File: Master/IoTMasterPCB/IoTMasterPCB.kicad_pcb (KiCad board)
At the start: 4 copper layers, 139 parts, among them J1 M50-3610742R, J2 10118194-0001LF, J3 RJMG1BD3B8K1ANR, U1 STM32F469IITx, U2 MYRGP330100B21RA, U3 CLRC66303HNY, U4 AT86RF232-ZX, U5 MIC826TYMT-TR, U6 KSZ8081MNX, U7 W25Q32JVSS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

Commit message: Placed STM32 on Master PCB. Corrected I2C naming.
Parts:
- moved R19 130.0 mm to (161.7, 60.6), turned to 180 degrees
- moved C18 128.4 mm to (161.7, 59.1)
- moved C5 125.6 mm to (155.5, 52.4), turned to 180 degrees
- moved J1 125.5 mm to (173.9, 75.0), turned to 90 degrees
- moved U1 123.1 mm to (146.4, 68.4), turned to 270 degrees
- moved C3 118.0 mm to (141.4, 53.9)
- moved C4 113.5 mm to (155.5, 53.9), turned to 180 degrees
- moved C16 112.6 mm to (160.9, 71.4), turned to 90 degrees
- moved X1 111.3 mm to (142.1, 49.8), turned to 270 degrees
- moved U7 111.1 mm to (173.8, 62.7), turned to 180 degrees
- moved R20 109.3 mm to (168.7, 71.7), turned to 270 degrees
- moved R16 109.1 mm to (161.7, 62.6), turned to 180 degrees
- moved C17 108.2 mm to (160.9, 66.4), turned to 90 degrees
- moved C2 105.3 mm to (155.4, 83.7), turned to 90 degrees
- moved C15 104.2 mm to (160.9, 77.9), turned to 90 degrees
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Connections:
- D1 pad 1: +5V -> Net-(D1-Pad1)
- D1 pad 2: GND -> GND1
- FB1 pad 2: Net-(FB1-Pad2) -> Net-(D1-Pad1)
- J2 pad 1: Net-(FB1-Pad2) -> Net-(D1-Pad1)
- R22 pad 1: /RFID/I2C_SDA -> /MCU/I2C2_SDA
- R23 pad 1: /RFID/I2C_SCL -> /MCU/I2C2_SCL
- U3 pad 29: /RFID/I2C_SCL -> /MCU/I2C2_SCL
- U3 pad 31: /RFID/I2C_SDA -> /MCU/I2C2_SDA
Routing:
- net +3V3: track 0.00 -> 37.9 mm
- net /RFID/PDOWN: track 0.00 -> 30.6 mm, vias 0 -> 2
- net /MCU/I2C2_SCL: track 0.00 -> 22.5 mm, vias 0 -> 2
- net /MCU/I2C2_SDA: track 0.00 -> 21.3 mm
- net /RFID/IRQ: track 0.00 -> 21.2 mm, vias 0 -> 2
- net /RFID/NFC_3V3: track 19.5 -> 29.5 mm
- net Net-(R24-Pad2): track 0.00 -> 9.60 mm
- net /MCU/12DSI: track 0.00 -> 7.54 mm
- net /MCU/VDDA: track 0.00 -> 6.82 mm
- net Net-(R25-Pad2): track 0.00 -> 6.29 mm
- net Net-(FL1-Pad3): track 0.00 -> 5.49 mm
- net Net-(FL1-Pad2): track 0.00 -> 5.47 mm
- net /MCU/NRST: track 0.00 -> 5.14 mm
- net /MCU/OSC_IN: track 0.00 -> 4.66 mm
- net Net-(D1-Pad1): track 0.00 -> 2.27 mm
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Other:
- board outline added: 170.2 x 81.2 mm

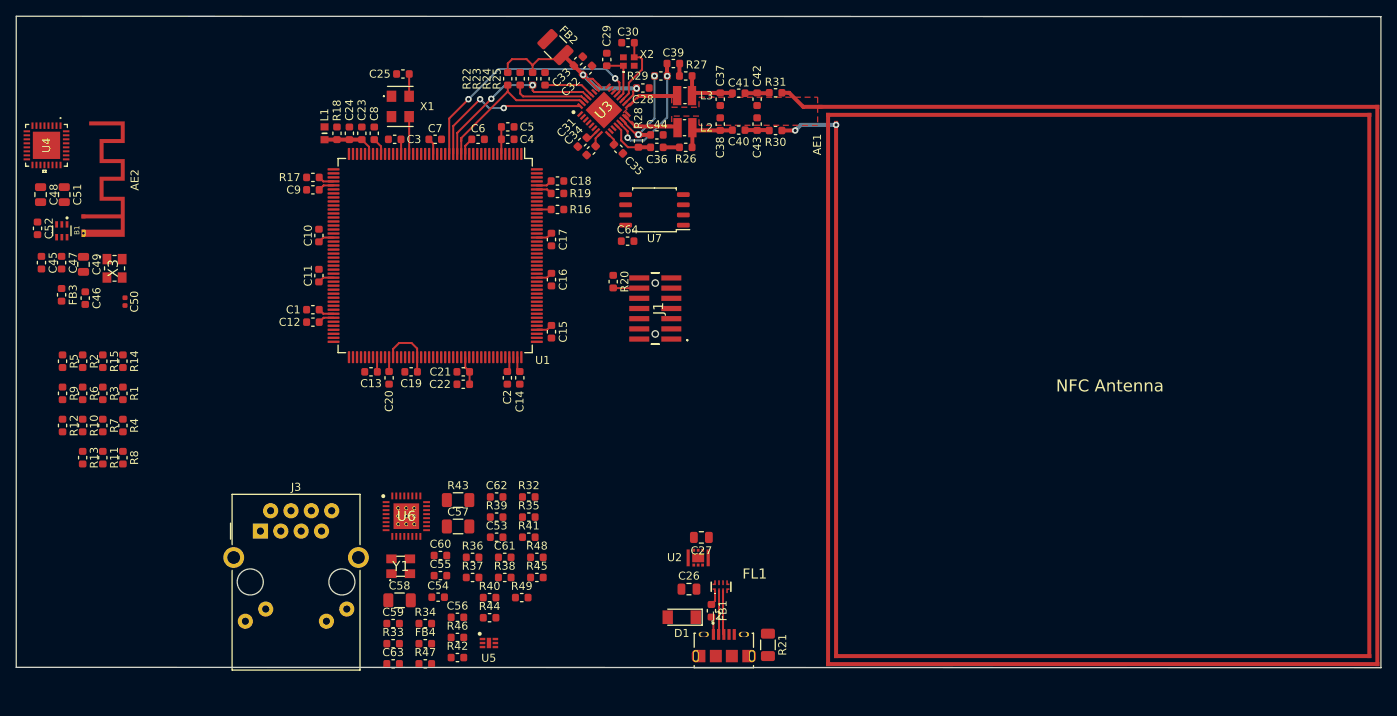
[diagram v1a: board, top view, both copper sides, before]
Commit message: More work on PCB layout, as wel as generation of LWIP (Ethernet) demo program for Master.
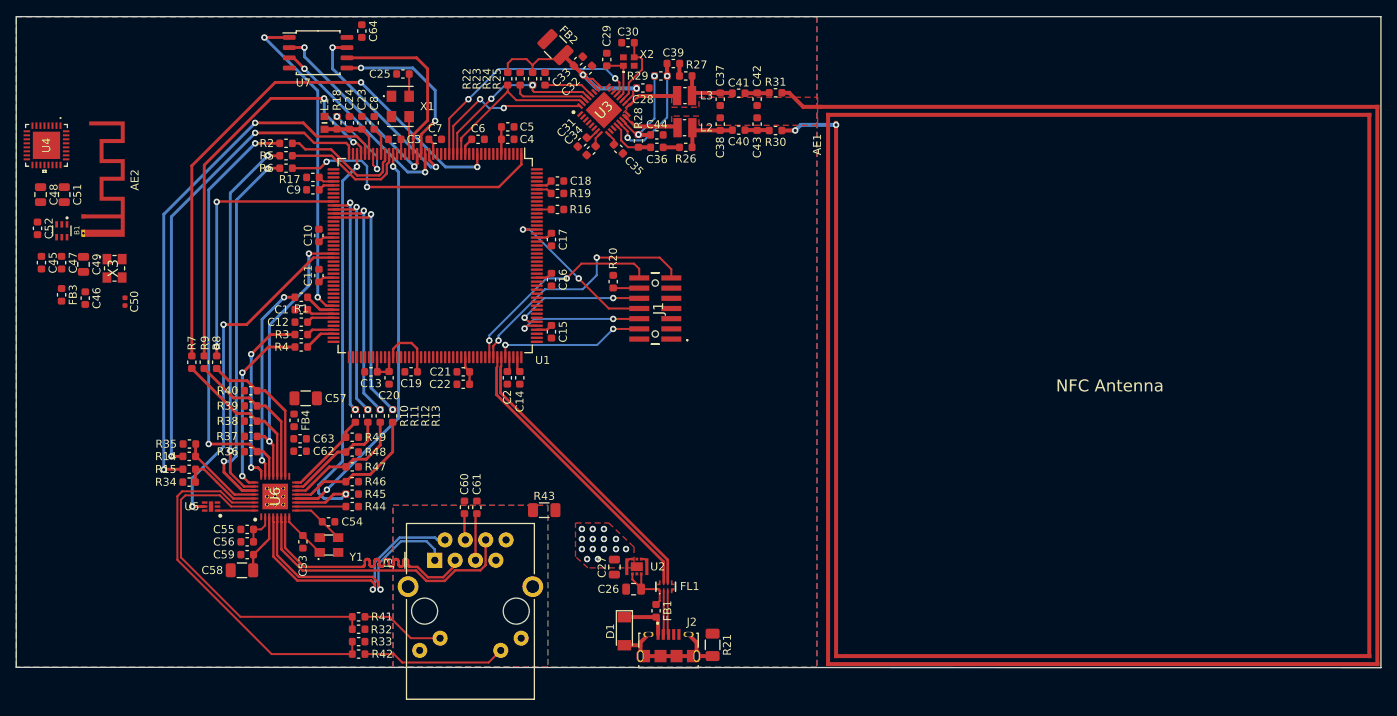
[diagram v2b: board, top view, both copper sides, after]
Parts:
- moved U7 46.3 mm to (131.8, 43.1), turned to 0 degrees
- moved R35 43.3 mm to (115.8, 91.9)
- moved C64 42.3 mm to (137.3, 40.4), turned to 270 degrees
- moved R12 39.6 mm to (139.6, 88.4)
- moved R40 39.4 mm to (123.5, 85.3)
- moved R13 39.0 mm to (141.2, 88.4)
- moved U5 38.6 mm to (118.5, 99.7), turned to 180 degrees
- moved R5 37.9 mm to (127.8, 56.0), turned to 180 degrees
- moved R6 37.8 mm to (127.8, 57.5), turned to 180 degrees
- moved R38 37.2 mm to (123.5, 89.0)
- moved R2 37.2 mm to (127.8, 54.4), turned to 180 degrees
- moved R34 34.3 mm to (115.8, 96.7)
- moved R10 34.0 mm to (136.5, 88.4)
- moved R39 33.7 mm to (123.5, 87.2)
- moved R11 33.5 mm to (138.1, 88.4)
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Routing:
- net /MCU/ETH_RX_ER: track 0.00 -> 69.6 mm, vias 0 -> 2
- net /MCU/ETH_CRS: track 0.00 -> 66.4 mm, vias 0 -> 2
- net /MCU/ETH_COL: track 0.00 -> 59.5 mm, vias 0 -> 2
- net /MCU/ETH_MDIO: track 0.00 -> 54.9 mm, vias 0 -> 2
- net /Ethernet/TX_CLK: track 0.00 -> 53.5 mm, vias 0 -> 2
- net /MCU/ETH_RX_CLK: track 0.00 -> 51.2 mm, vias 0 -> 2
- net /MCU/ETH_MDC: track 0.00 -> 50.2 mm, vias 0 -> 2
- net /Ethernet/TXD3: track 0.00 -> 47.0 mm, vias 0 -> 2
- net /Ethernet/TXD2: track 0.00 -> 46.8 mm, vias 0 -> 2
- net /Ethernet/LED1: track 0.00 -> 46.7 mm
- net /Ethernet/LED2: track 0.00 -> 43.2 mm
- net /MCU/~ETH_RESET: track 0.00 -> 43.0 mm, vias 0 -> 2
- net /MCU/~QSPI_BK1_NCS: track 0.00 -> 40.7 mm, vias 0 -> 2
- net /MCU/USB_DP: track 0.00 -> 36.8 mm
- net /MCU/USB_DN: track 0.00 -> 36.8 mm
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- added copper zone on F.Cu, net +3V3
- added copper zone on Supply.Cu, net +3V3
- added copper zone on B.Cu, net GND
- added copper zone on Ground.Cu, net GND
- added copper zone on B.Cu, net Net-(J3-Pad13)
- added copper zone on F.Cu, net Net-(J3-Pad13)
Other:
- outline, holes or cut-outs redrawn
- net class Default: clearance 0.2 -> 0.155
- net class Ethernet added: clearance 0.155, trace_width 0.36, via_dia 0.8, via_drill 0.4
- net class USB added: clearance 0.15, trace_width 0.25, via_dia 0.8, via_drill 0.4
- rule trace_clearance: 0.2 -> 0.155

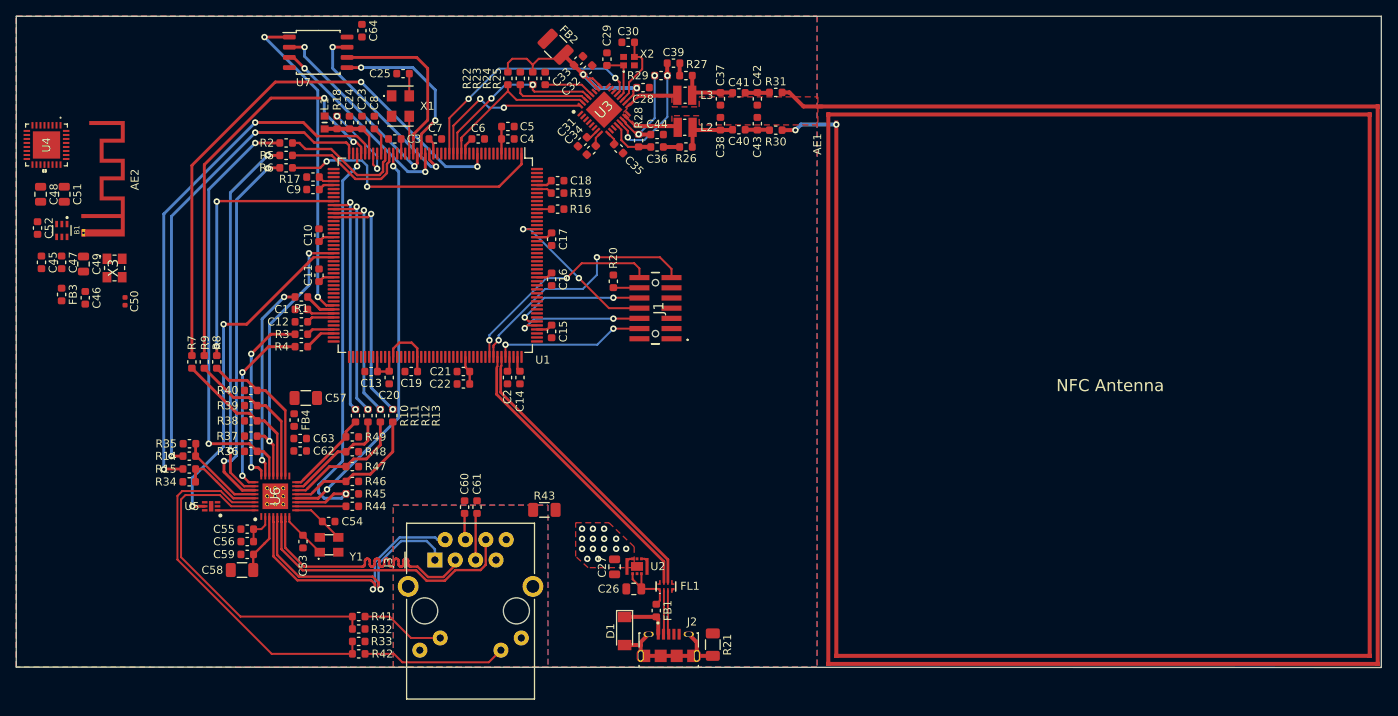
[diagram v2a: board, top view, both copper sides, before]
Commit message: Minor changes to schematic, finished placing all components, only minor fixes needed to PCB now.
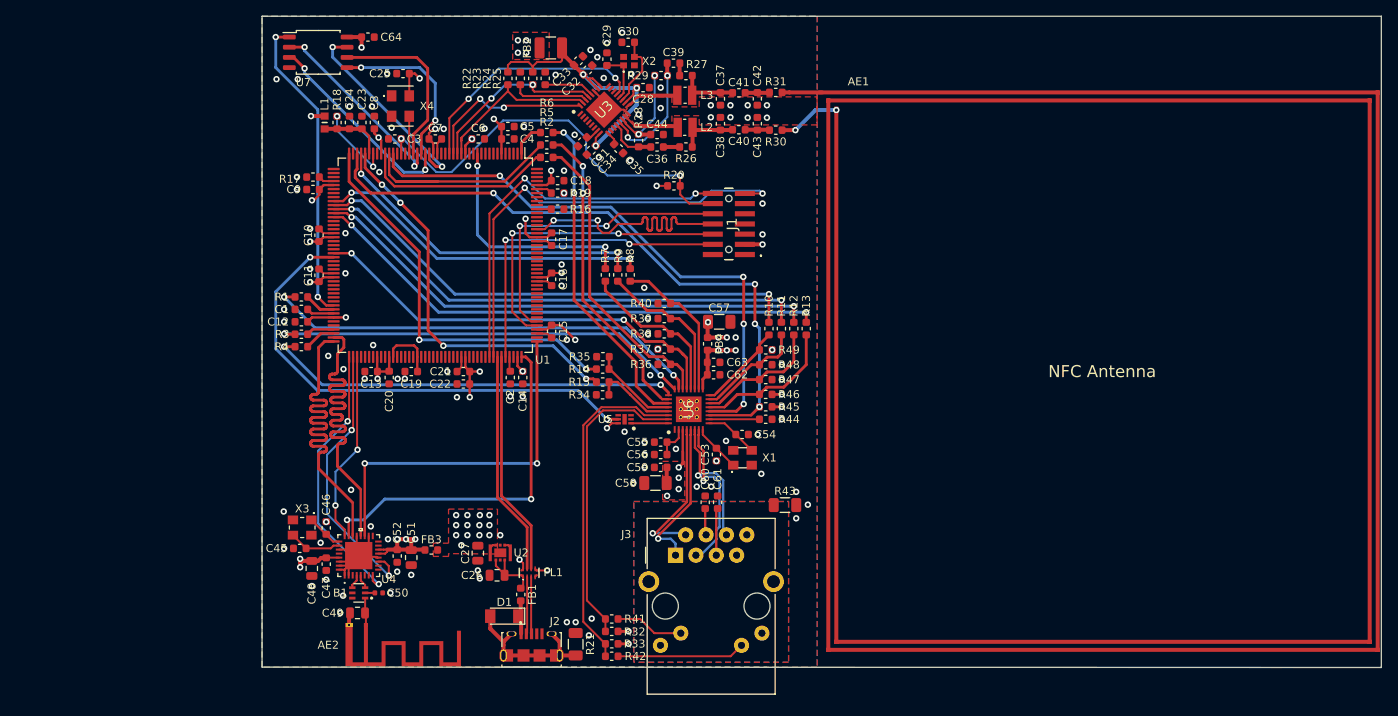
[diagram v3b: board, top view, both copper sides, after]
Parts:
- J3: footprint Connector_RJ:RJ45_Amphenol_RJMG1BD3B8K1ANR -> Personal_Misc:RJMG1BD3B8K1ANR
- moved U4 64.3 mm to (136.9, 105.8), turned to 90 degrees
- moved C51 62.6 mm to (143.4, 106.1)
- moved AE2 62.0 mm to (137.8, 114.5), turned to 180 degrees
- moved C52 60.7 mm to (141.7, 105.9)
- moved B1 58.4 mm to (136.9, 110.5), turned to 180 degrees
- moved C48 57.6 mm to (131.1, 107.5), turned to 90 degrees
- moved FB3 56.0 mm to (145.9, 105.2), turned to 0 degrees
- moved C49 55.3 mm to (136.8, 113.0), turned to 180 degrees
- moved C53 52.7 mm to (181.5, 93.2)
- moved C55 52.7 mm to (174.6, 91.7)
- moved C56 52.7 mm to (174.6, 93.2)
- moved C58 52.7 mm to (173.9, 96.8)
- moved C59 52.7 mm to (174.6, 94.8)
- moved R10 52.7 mm to (188.1, 77.5)
- moved R12 52.7 mm to (191.2, 77.5)
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- renumbered Y1 to X1, X1 to X4
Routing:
- net /MCU/NRST: track 5.14 -> 52.0 mm, vias 0 -> 2
- net GND: track 0.00 -> 46.7 mm, vias 0 -> 103
- net /MCU/SPI2_SCK: track 0.00 -> 45.7 mm, vias 0 -> 2
- net /MCU/SPI2_MISO: track 0.00 -> 45.1 mm
- net /MCU/~SPI2_NSS: track 0.00 -> 44.6 mm, vias 0 -> 2
- net /MCU/SPI2_MOSI: track 0.00 -> 44.0 mm
- net /MCU/ETH_RX_ER: track 69.6 -> 29.4 mm
- net +3V3: track 43.6 -> 81.9 mm, vias 14 -> 43
- net /MCU/ETH_RXD3: track 30.3 -> 65.1 mm
- net /ZigBee/~RST: track 0.00 -> 34.7 mm, vias 0 -> 2
- net /MCU/ETH_RXD2: track 29.6 -> 64.2 mm
- net /MCU/ETH_RXD0: track 28.3 -> 62.8 mm
- net /ZigBee/SLP_TR: track 0.00 -> 34.5 mm, vias 0 -> 2
- net /MCU/ETH_RXD1: track 28.8 -> 63.3 mm
- net /Ethernet/TX_EN: track 25.0 -> 55.9 mm
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- added copper zone on F.Cu, net /Ethernet/VDDA
- added copper zone on Supply.Cu, net /Ethernet/VDDA
- added copper zone on Supply.Cu, net /ZigBee/ZB_3V3
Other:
- board size 170.2 x 81.2 mm -> 139.5 x 81.2 mm

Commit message: Finished Master PCB layout. Added revised LWIP Master Demo for STM32F769 discovery board, which has been confirmed to work by setting up at web page.
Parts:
- moved B1 0.33 mm to (136.9, 110.8)
- moved C50 0.33 mm to (139.4, 110.8)
- moved C49 0.08 mm to (136.8, 113.1)
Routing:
- net /MCU/ETH_RX_DV: track 42.1 -> 60.0 mm
- net /MCU/ETH_RX_CLK: track 40.6 -> 58.4 mm
- net /MCU/ETH_RX_ER: track 29.4 -> 44.5 mm
- net /Ethernet/TXD3: track 41.6 -> 55.4 mm
- net /MCU/JTDO: track 33.9 -> 24.6 mm
- net GND: track 46.7 -> 52.6 mm, vias 103 -> 193
- net /Ethernet/RX_ER: track 20.0 -> 24.7 mm
- net /MCU/ETH_TXD2: track 29.0 -> 24.3 mm
- net /MCU/ETH_TX_CLK: track 24.3 -> 25.5 mm
- net (no net): track 0.00 -> 0.95 mm
- net Net-(J3-Pad13): vias 0 -> 1
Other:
- board text added: "IoT Project Master Version 1, 2021 Sebastian Madsen"
- board text added: "ZigBee Antenna"

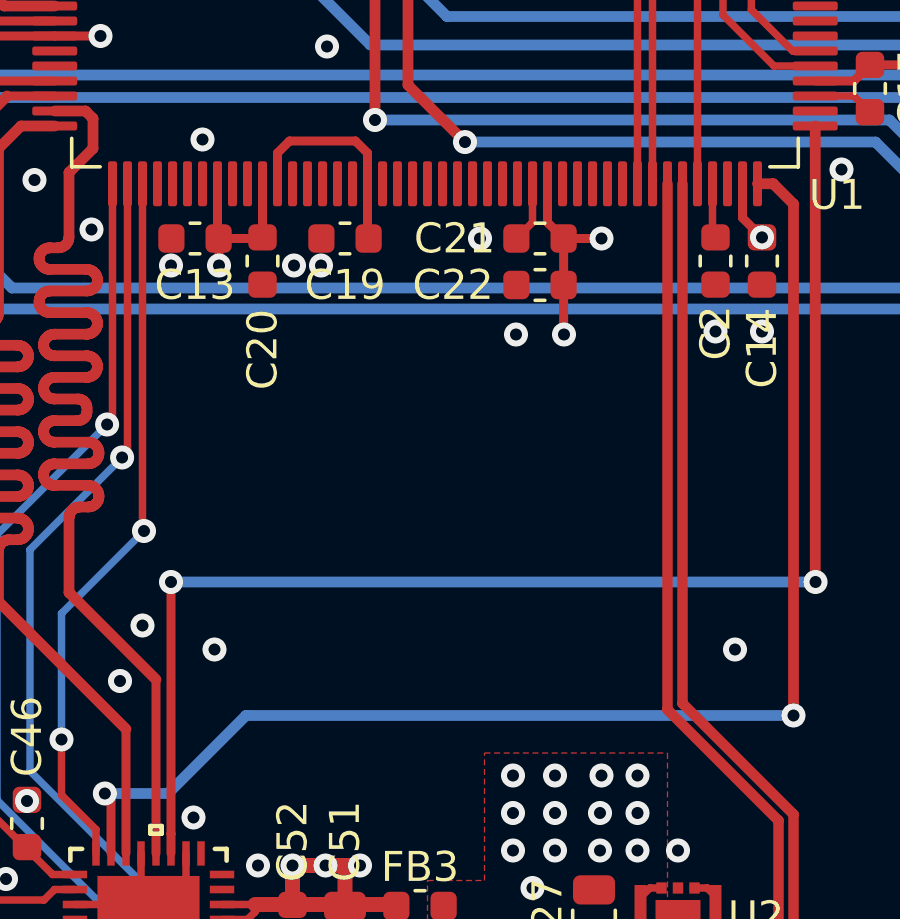
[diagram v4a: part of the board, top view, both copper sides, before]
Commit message: Added further documentation in ReadMe. Added status LEDs to Master.
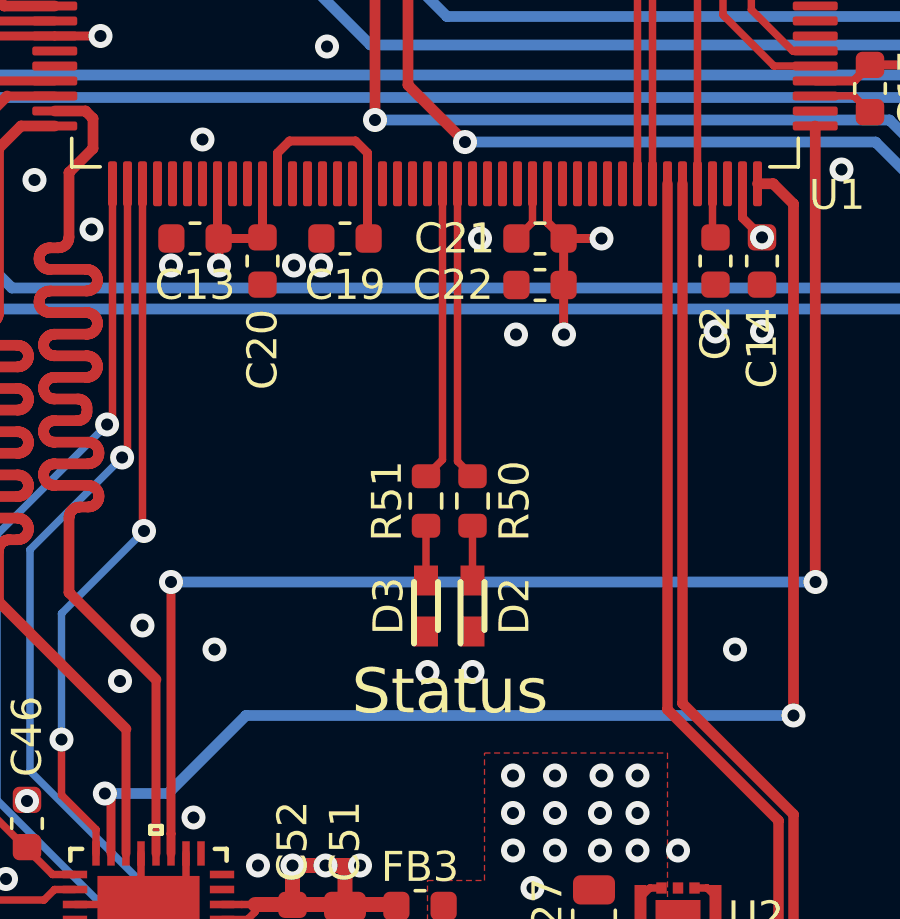
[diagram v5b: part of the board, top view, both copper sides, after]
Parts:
- added D2: 150060SS55040, Personal_Passives:150060VS55040, F.Cu at (147.7, 95.2)
- added D3: 150060VS55040, Personal_Passives:150060VS55040, F.Cu at (146.2, 95.2)
- added R50: 150, Resistor_SMD:R_0603_1608Metric, F.Cu at (147.7, 91.7)
- added R51: 150, Resistor_SMD:R_0603_1608Metric, F.Cu at (146.2, 91.7)
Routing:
- net Net-(R51-Pad2): track 0.00 -> 9.98 mm
- net Net-(R50-Pad2): track 0.00 -> 9.96 mm
- net Net-(D3-Pad2): track 0.00 -> 1.83 mm
- net Net-(D2-Pad2): track 0.00 -> 1.83 mm
- net GND: vias 193 -> 195
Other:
- board text added: "Status"
